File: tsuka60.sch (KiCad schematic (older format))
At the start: 178 parts, among them SW1 SW_Push, U1 ATmega32U4-AU, Y1 Resonator_Small

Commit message: removed lots of compatibility
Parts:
- removed D67: D_Small, Diode_SMD:D_0805_2012Metric, symbol Device:D_Small
- removed MX37: LEGACY-H, MX_Alps_Hybrid:MX-1U-NoLED, symbol MX_Alps_Hybrid:MX-NoLED
- removed MX65-3: SPACE, MX_Alps_Hybrid:MX-6.25U-ReversedStabilizers-NoLED, symbol MX_Alps_Hybrid:MX-NoLED
- removed MX67-3: LEGACY-BOTTOM, MX_Alps_Hybrid:MX-1.25U-NoLED, symbol MX_Alps_Hybrid:MX-NoLED
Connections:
- net Col3: now also MX64-ALPS-1.2 (ROW); no longer MX64-ALPS-1.1 (COL)
- net Col5: now also MX66-ALPS-1.2 (ROW); no longer MX66-ALPS-1.1 (COL)
- net Col7: now also MX38.1 (COL); no longer MX38.2 (ROW)
- net at D64.2 (A), MX64-1.2 (ROW), MX64-2.2 (ROW): now also MX64-ALPS-1.1 (COL); no longer MX64-ALPS-1.2 (ROW)
- net at D38.2 (A): now also MX38.2 (ROW); no longer MX38.1 (COL)
- net at D66.2 (A), MX66-1.2 (ROW), MX66-2.2 (ROW): now also MX66-ALPS-1.1 (COL); no longer MX66-ALPS-1.2 (ROW)
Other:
- moved on the sheet: MX38, MX64-ALPS-1, MX66-ALPS-1
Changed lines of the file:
@@
 L MX_Alps_Hybrid:MX-NoLED MX38
 U 1 1 5DDC2D4A
-P 11650 4650
-F 0 "MX38" H 11732 4874 60  0000 C CNN
-F 1 "BACKSPACE" H 11732 4800 20  0000 C CNN
-F 2 "MX_Alps_Hybrid:MX-1.5U-NoLED" H 11025 4625 60  0001 C CNN
-F 3 "" H 11025 4625 60  0001 C CNN
-	1    11650 4650
-	0    1    1    0
+P 11350 4650
+F 0 "MX38" H 11432 4874 60  0000 C CNN
+F 1 "BACKSPACE" H 11432 4800 20  0000 C CNN
+F 2 "MX_Alps_Hybrid:MX-1.5U-NoLED" H 10725 4625 60  0001 C CNN
+F 3 "" H 10725 4625 60  0001 C CNN
+	1    11350 4650
+	1    0    0    -1
 $EndComp
 $Comp
@@
 	1500 3750 2400 3750
 Connection ~ 11150 5000
-Wire Wire Line
-	11500 3350 11500 4125
 $Comp
 L MX_Alps_Hybrid:MX-NoLED MX39
@@
 Wire Wire Line
 	20250 3350 20250 4600
-Wire Wire Line
-	9900 9275 12400 9275
-$Comp
-L MX_Alps_Hybrid:MX-NoLED MX65-3
-U 1 1 5E334ECE
-P 7600 8150
-F 0 "MX65-3" H 7682 8374 60  0000 C CNN
-F 1 "SPACE" H 7682 8300 20  0000 C CNN
-F 2 "MX_Alps_Hybrid:MX-6.25U-ReversedStabilizers-NoLED" H 6975 8125 60  0001 C CNN
-F 3 "" H 6975 8125 60  0001 C CNN
-	1    7600 8150
-	1    0    0    -1
-$EndComp
 $Comp
 L MX_Alps_Hybrid:MX-NoLED MX65-2
@@
 Wire Wire Line
 	7400 9275 8650 9275
-Wire Wire Line
-	8650 9275 9900 9275
 $Comp
 L MX_Alps_Hybrid:MX-NoLED MX66-2
@@
 $EndComp
 $Comp
-L MX_Alps_Hybrid:MX-NoLED MX67-3
-U 1 1 5DDF3CC5
-P 10100 8150
-F 0 "MX67-3" H 10182 8374 60  0000 C CNN
-F 1 "LEGACY-BOTTOM" H 10182 8300 20  0000 C CNN
-F 2 "MX_Alps_Hybrid:MX-1.25U-NoLED" H 9475 8125 60  0001 C CNN
-F 3 "" H 9475 8125 60  0001 C CNN
-	1    10100 8150
-	1    0    0    -1
-$EndComp
-$Comp
 L Device:D_Small D63
 U 1 1 5D97857A
@@
 $EndComp
 $Comp
-L Device:D_Small D67
-U 1 1 5D9785AE
-P 9900 9175
-F 0 "D67" V 9950 9575 50  0000 R CNN
-F 1 "D_Small" V 9850 9575 50  0000 R CNN
-F 2 "Diode_SMD:D_0805_2012Metric" V 9900 9175 50  0001 C CNN
-F 3 "~" V 9900 9175 50  0001 C CNN
-	1    9900 9175
-	0    -1   -1   0
-$EndComp
-Connection ~ 9900 9275
-$Comp
 L Device:D_Small D69
 U 1 1 5D9785C8
@@
 Connection ~ 9000 5850
 Wire Wire Line
-	10250 5850 10250 8100
-Connection ~ 10250 5850
-Wire Wire Line
 	20250 5850 20250 8600
 Connection ~ 20250 5850
@@
 Wire Wire Line
 	6500 7100 6500 7600
-Connection ~ 7750 7600
-Wire Wire Line
-	7750 7600 7750 8100
 Connection ~ 7750 7100
-Wire Wire Line
-	7750 7100 7750 7600
 Connection ~ 7750 6600
 Wire Wire Line
@@
 Connection ~ 12400 7300
 Wire Wire Line
-	9900 9075 9900 8300
-Wire Wire Line
-	9900 8300 10050 8300
-Wire Wire Line
 	8650 9075 8650 8800
 Wire Wire Line
@@
 	7400 7300 7400 7800
 Connection ~ 7400 7800
-Wire Wire Line
-	7550 8300 7400 8300
-Wire Wire Line
-	7400 7800 7400 8300
-Connection ~ 7400 8300
-Wire Wire Line
-	7400 8300 7400 9075
 Wire Wire Line
 	6150 7300 6300 7300
@@
 Wire Wire Line
 	19000 4000 19000 4600
-$Comp
-L MX_Alps_Hybrid:MX-NoLED MX37
-U 1 1 5DDB767A
-P 11200 4175
-F 0 "MX37" H 11282 4399 60  0000 C CNN
-F 1 "LEGACY-H" H 11282 4325 20  0000 C CNN
-F 2 "MX_Alps_Hybrid:MX-1U-NoLED" H 10575 4150 60  0001 C CNN
-F 3 "" H 10575 4150 60  0001 C CNN
-	1    11200 4175
-	1    0    0    -1
-$EndComp
 Wire Wire Line
 	10250 3350 10250 5850
-Connection ~ 11500 4125
-Wire Wire Line
-	11350 4125 11500 4125
 Wire Wire Line
 	8650 5000 11150 5000
 Wire Wire Line
-	11150 4325 11150 4800
-Connection ~ 11150 4800
-Wire Wire Line
-	11500 4125 11500 4600
-Connection ~ 11500 4600
-Wire Wire Line
-	11500 4600 11500 5850
-Wire Wire Line
-	11150 4800 11700 4800
+	11150 4800 11300 4800
 Text GLabel 5325 14525 2    50   Input ~ 0
 Col0
@@
 L MX_Alps_Hybrid:MX-NoLED MX64-ALPS-1
 U 1 1 5E969378
-P 6350 8650
-F 0 "MX64-ALPS-1" H 6432 8874 60  0000 C CNN
-F 1 "SPACE LEFT" H 6432 8800 20  0000 C CNN
-F 2 "MX_Alps_Hybrid:MX-2.75U-NoLED" H 5725 8625 60  0001 C CNN
-F 3 "" H 5725 8625 60  0001 C CNN
-	1    6350 8650
-	1    0    0    -1
+P 6650 8650
+F 0 "MX64-ALPS-1" H 6732 8874 60  0000 C CNN
+F 1 "SPACE LEFT" H 6732 8800 20  0000 C CNN
+F 2 "MX_Alps_Hybrid:MX-2.75U-NoLED" H 6025 8625 60  0001 C CNN
+F 3 "" H 6025 8625 60  0001 C CNN
+	1    6650 8650
+	0    1    1    0
 $EndComp
 $Comp
 L MX_Alps_Hybrid:MX-NoLED MX66-ALPS-1
 U 1 1 5E96C8F7
-P 8850 8650
-F 0 "MX66-ALPS-1" H 8932 8874 60  0000 C CNN
-F 1 "SPACE RIGHT" H 8932 8800 20  0000 C CNN
-F 2 "MX_Alps_Hybrid:MX-2.75U-NoLED" H 8225 8625 60  0001 C CNN
-F 3 "" H 8225 8625 60  0001 C CNN
-	1    8850 8650
-	1    0    0    -1
+P 9150 8650
+F 0 "MX66-ALPS-1" H 9232 8874 60  0000 C CNN
+F 1 "SPACE RIGHT" H 9232 8800 20  0000 C CNN
+F 2 "MX_Alps_Hybrid:MX-2.75U-NoLED" H 8525 8625 60  0001 C CNN
+F 3 "" H 8525 8625 60  0001 C CNN
+	1    9150 8650
+	0    1    1    0
 $EndComp
 Wire Wire Line
 	9000 7600 9000 8600
 Connection ~ 9000 7600
-Wire Wire Line
-	8800 8800 8650 8800
 Connection ~ 8650 8800
 Wire Wire Line
@@
 	6500 8600 6500 7600
 Connection ~ 6500 7600
-Wire Wire Line
-	6300 8800 6150 8800
 Connection ~ 6150 8800
 Wire Wire Line
 	6150 8800 6150 9075
+Wire Wire Line
+	8650 8800 9200 8800
+Wire Wire Line
+	8650 9275 12400 9275
+Wire Wire Line
+	7400 7800 7400 9075
+Wire Wire Line
+	7750 7100 7750 7600
+Wire Wire Line
+	6150 8800 6700 8800
+Wire Wire Line
+	11500 3350 11500 4600
+Connection ~ 11500 4600
+Wire Wire Line
+	11500 4600 11500 5850
 $EndSCHEMATC

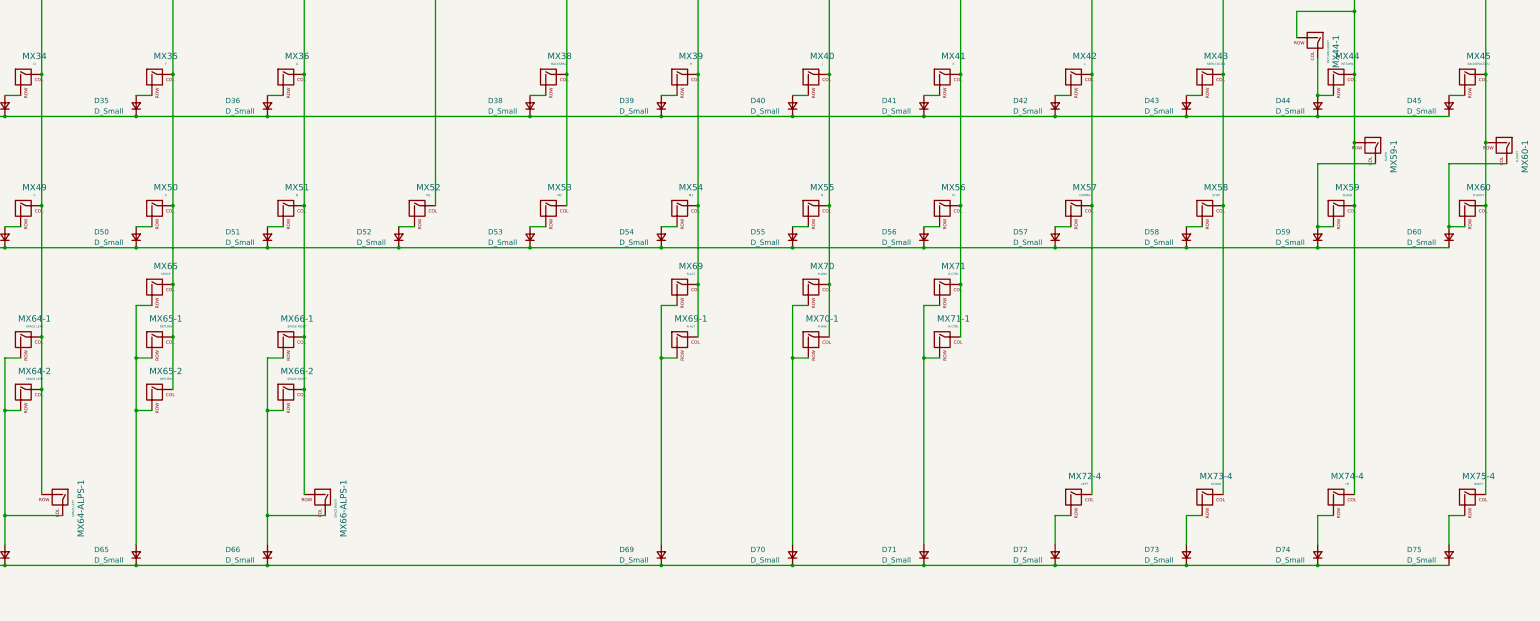
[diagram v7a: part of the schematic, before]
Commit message: Adjusted bottom row. Need to add a new bottom row for the Colemak Forum people.
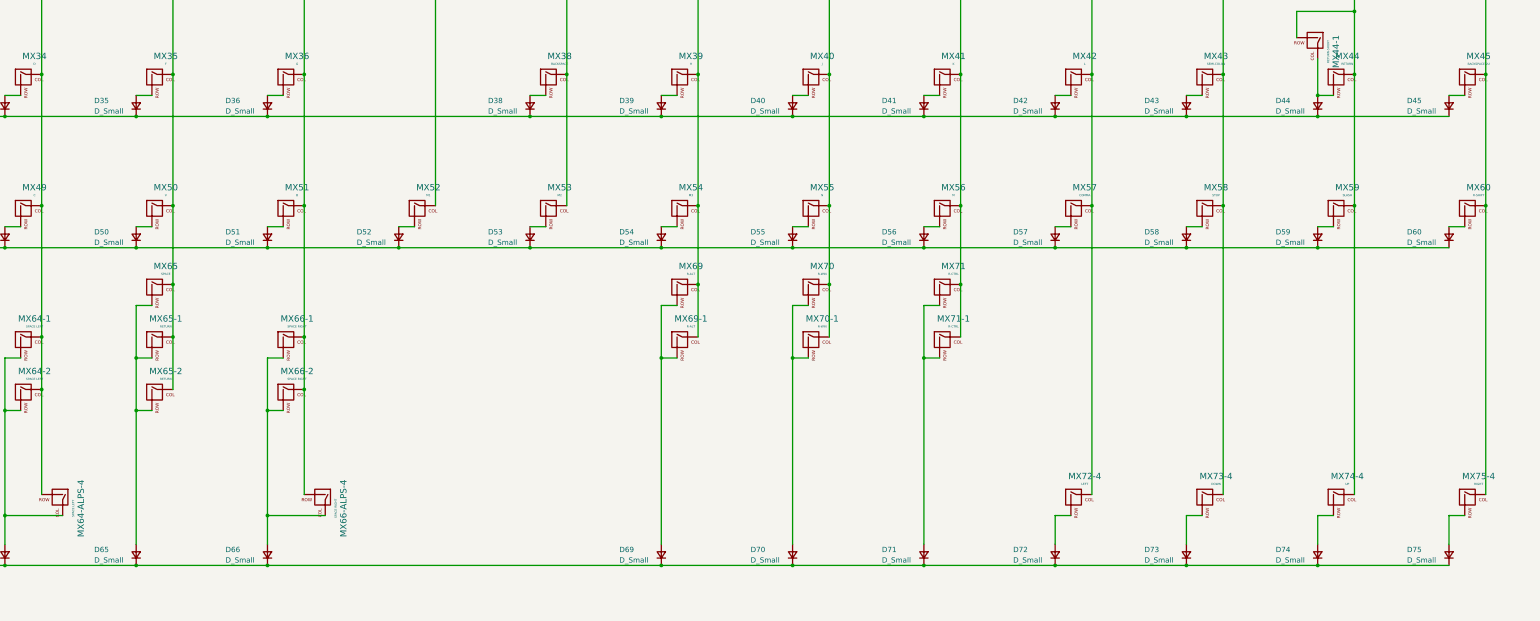
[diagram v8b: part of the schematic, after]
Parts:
- removed MX59-1: SLASH, MX_Alps_Hybrid:MX-1.5U-NoLED, symbol MX_Alps_Hybrid:MX-NoLED
- removed MX60-1: R-SHIFT, MX_Alps_Hybrid:MX-1U-NoLED, symbol MX_Alps_Hybrid:MX-NoLED
- renumbered MX64-ALPS-1 to MX64-ALPS-4, MX66-ALPS-1 to MX66-ALPS-4
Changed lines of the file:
@@
 Connection ~ 19000 3350
 Connection ~ 19000 4600
-Wire Wire Line
-	19000 4600 19000 5250
 Connection ~ 17750 4600
 Wire Wire Line
@@
 	20250 2100 20250 3350
 Connection ~ 20250 4600
-Wire Wire Line
-	20250 4600 20250 5250
 Connection ~ 20250 2100
 Connection ~ 20250 3350
@@
 Col0
 $Comp
-L MX_Alps_Hybrid:MX-NoLED MX59-1
-U 1 1 5EBC7D92
-P 19150 5300
-F 0 "MX59-1" H 19232 5524 60  0000 C CNN
-F 1 "SLASH" H 19232 5450 20  0000 C CNN
-F 2 "MX_Alps_Hybrid:MX-1.5U-NoLED" H 18525 5275 60  0001 C CNN
-F 3 "" H 18525 5275 60  0001 C CNN
-	1    19150 5300
-	0    1    1    0
-$EndComp
-Connection ~ 19000 5250
-Wire Wire Line
-	19000 5250 19000 5850
-$Comp
-L MX_Alps_Hybrid:MX-NoLED MX60-1
-U 1 1 5EBC9271
-P 20400 5300
-F 0 "MX60-1" H 20482 5524 60  0000 C CNN
-F 1 "R-SHIFT" H 20482 5450 20  0000 C CNN
-F 2 "MX_Alps_Hybrid:MX-1U-NoLED" H 19775 5275 60  0001 C CNN
-F 3 "" H 19775 5275 60  0001 C CNN
-	1    20400 5300
-	0    1    1    0
-$EndComp
-Connection ~ 20250 5250
-Wire Wire Line
-	20250 5250 20250 5850
-Wire Wire Line
-	20450 5450 19900 5450
-Wire Wire Line
-	19900 5450 19900 6050
-Connection ~ 19900 6050
-Wire Wire Line
-	19200 5450 18650 5450
-Wire Wire Line
-	18650 5450 18650 6050
-Connection ~ 18650 6050
-$Comp
-L MX_Alps_Hybrid:MX-NoLED MX64-ALPS-1
+L MX_Alps_Hybrid:MX-NoLED MX64-ALPS-4
 U 1 1 5E969378
 P 6650 8650
-F 0 "MX64-ALPS-1" H 6732 8874 60  0000 C CNN
+F 0 "MX64-ALPS-4" H 6732 8874 60  0000 C CNN
 F 1 "SPACE LEFT" H 6732 8800 20  0000 C CNN
 F 2 "MX_Alps_Hybrid:MX-2.75U-NoLED" H 6025 8625 60  0001 C CNN
@@
 $EndComp
 $Comp
-L MX_Alps_Hybrid:MX-NoLED MX66-ALPS-1
+L MX_Alps_Hybrid:MX-NoLED MX66-ALPS-4
 U 1 1 5E96C8F7
 P 9150 8650
-F 0 "MX66-ALPS-1" H 9232 8874 60  0000 C CNN
+F 0 "MX66-ALPS-4" H 9232 8874 60  0000 C CNN
 F 1 "SPACE RIGHT" H 9232 8800 20  0000 C CNN
 F 2 "MX_Alps_Hybrid:MX-2.75U-NoLED" H 8525 8625 60  0001 C CNN
@@
 Wire Wire Line
 	11500 4600 11500 5850
+Wire Wire Line
+	19000 4600 19000 5850
+Wire Wire Line
+	20250 4600 20250 5850
 $EndSCHEMATC
